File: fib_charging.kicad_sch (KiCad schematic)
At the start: 50 parts, among them J301 Conn_01x02, J302 Conn_01x02, J303 Conn_01x02, Q301 CSD17581Q3A, Q302 CSD17581Q3A, Q303 CSD17581Q3A, Q304 CSD17581Q3A, U301 BQ25798RQMR

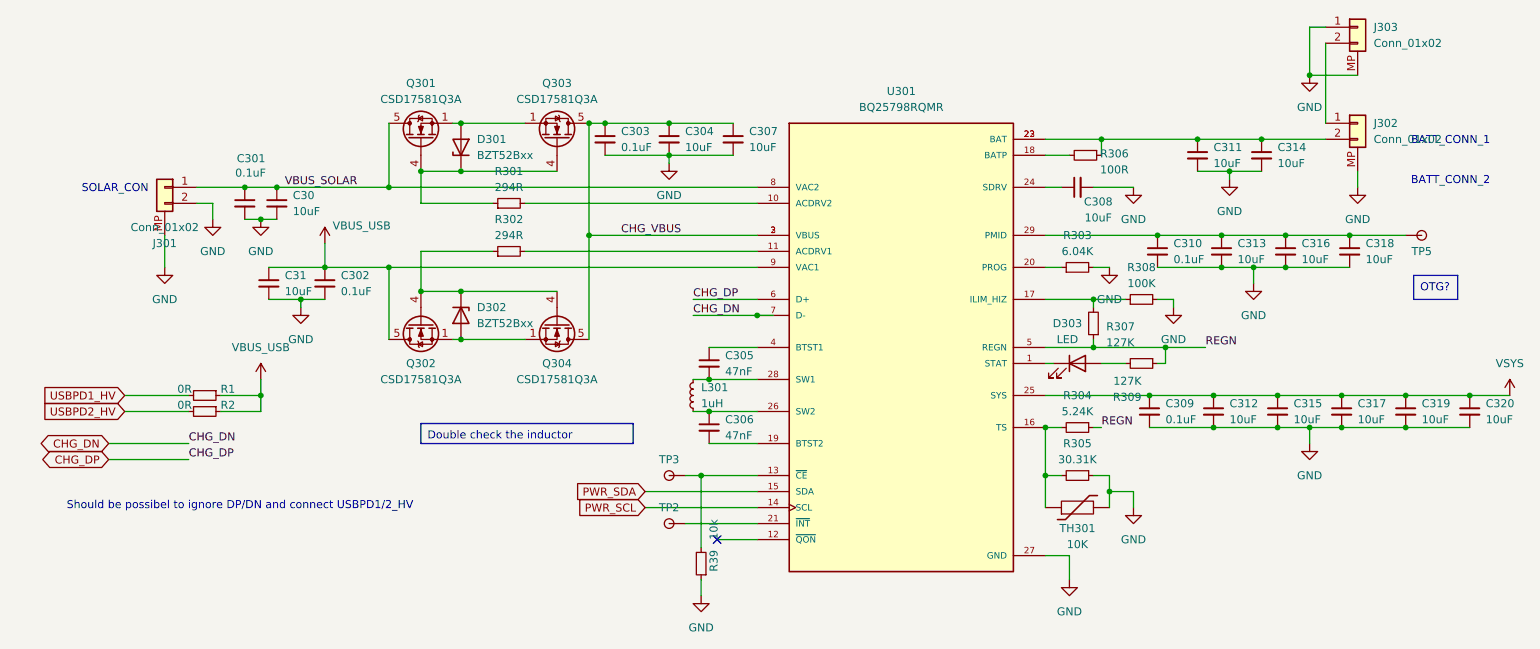
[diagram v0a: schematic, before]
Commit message: adde testpoints, fixed power supplies, ready to order
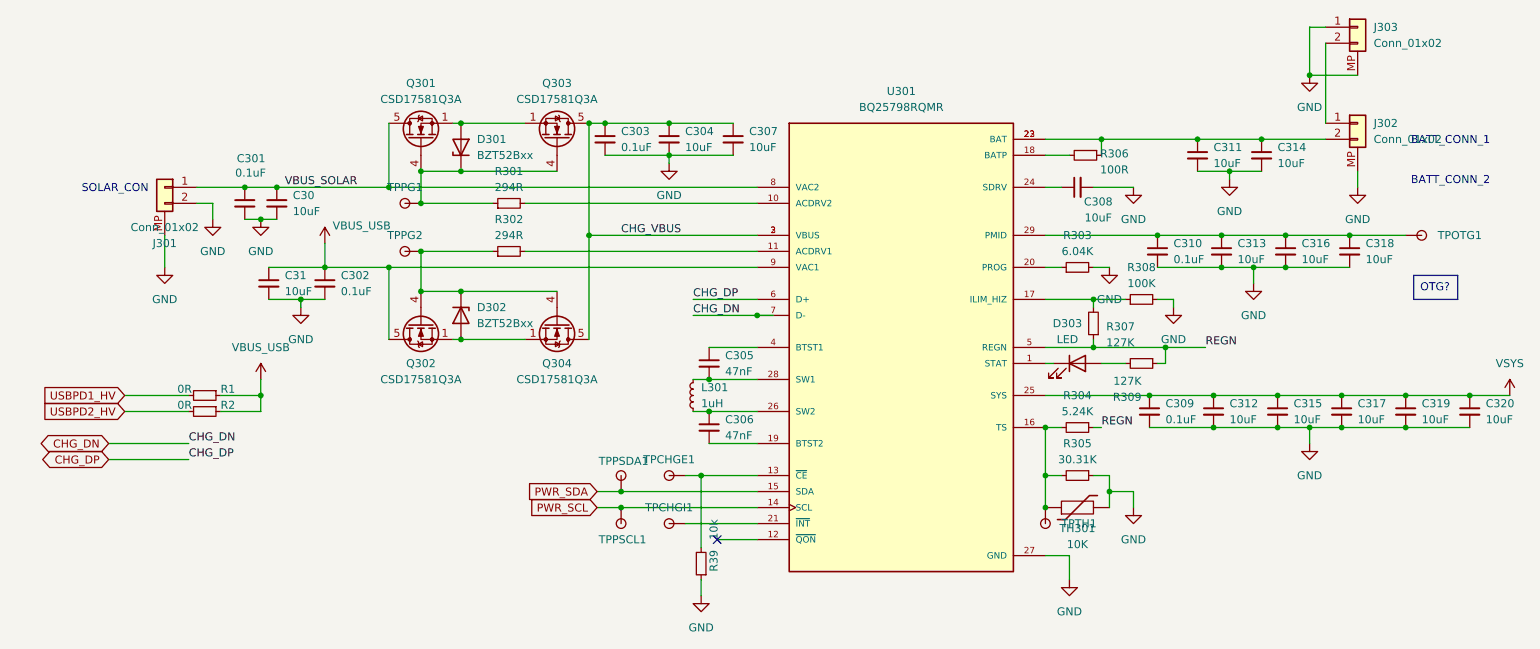
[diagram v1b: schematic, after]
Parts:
- added TPPG1, TPPG2, TPPSCL1, TPPSDA1, TPTH1: TestPoint, TestPoint:TestPoint_Pad_D1.0mm, symbol Fibel2:TestPoint
- renumbered TP3 to TPCHGE1, TP2 to TPCHGI1, TP5 to TPOTG1
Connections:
- net PWR_SCL: now also TPPSCL1.1
- net PWR_SDA: now also TPPSDA1.1
- net at D302.1 (K), Q302.4 (G), Q304.4 (G)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: now also TPPG2.1
- net at R304.2, R305.2, TH301.1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: now also TPTH1.1
- net at D301.1 (K), Q301.4 (G), Q303.4 (G)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: now also TPPG1.1
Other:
- note removed: "Should be possibel to ignore DP/DN and connect USBPD1/2_HV"
